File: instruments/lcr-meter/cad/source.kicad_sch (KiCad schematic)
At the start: 19 parts, among them U4 AD9833BRMZ-REEL7, U5 OPA810IDBVR

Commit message: lcr-meter Rev D: apply Tier 1 audit fixes
Hand-routed layout edits (cad/tools/edit_lib.py, no autorouter):
- Vias in every exposed pad: U1 8, U8/U9/U10 5, U11/U12 6 (were 0), U13 9.
- ADS9224R: 10 uF X7R 0805 reference caps at 1.56 mm, REFM joined to the
  cap before its via; 1 uF AVDD caps at 1.67/2.46 mm from pins 12/29.
- TPS7A4901/TPS7A3001: support parts packed per TI layout; FB nodes
  13.2/12.0 -> 5.2/5.3 mm, NR 2.1 mm. LDOIN_N In2 run moved off the pads.
- TPS65131 dividers compacted: CONV_FBP 13.1 -> 9.1 mm, CONV_FBN 16.8 -> 12.3 mm.
- RP2040: 1 uF at VREG_VIN (C5).

Parts: red status LED, basic ferrites, W25Q128JV flash (stock), C84,
CL32B106KBJNNNE on the 14 V and converter-input caps, C18/C103 basic,
C36 1 uF -> 100 nF. Extended lines 34 -> 30.

Firmware: settle max(150 ms, 20 cycles); BOOT -> reset_usb_boot().
Host 0.7.0: `temper-lcr boot PORT`.

Withdrawn after checking: converter dividers to TI example values (VPOS
15.105 V at the tolerance stack), 1 % LDO dividers (U12 headroom 0.74 V),
SRV05-4 (pinout unverifiable). regulator_check.py now reads design.json
instead of stale Rev C values.

DRC 0, unconnected 0, parity 0, ERC 0; independent check 576 pins, 0
findings; host 29 tests pass.

Co-Authored-By: Claude Opus 5.5 <noreply@anthropic.com>
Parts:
- C36: value 1uF 50V -> 100nF 50V; LCSC C28323 -> C49678; MPN CL21B105KBFNNNE -> CC0805KRX7R9BB104; Manufacturer Samsung Electro-Mechanics -> YAGEO; Unit_USD 0.0344 -> 0.015
- FB2: value 120R@100MHz 3A -> 100R@100MHz 800mA; LCSC C79382 -> C1015; MPN BLM21PG121SN1D -> GZ2012D101TF; Manufacturer Murata Electronics -> Sunlord; Unit_USD 0.0406 -> 0.0311

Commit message: feat(lcr): Rev E board with TAC5112 codec front end and relay ranges
Hand-routed Rev E on the Rev D outline:
- removes the ADS9224R, AD9833, both THS4551s, FB2 and JP1-JP6;
- adds the TAC5112 with its own AP2112K for 3V3A, three TQ2SA latching
  relays and their AO3400A drivers.

cad/tools/rev_e.py builds design.json and routing.json from the Rev D
package. rev_e_routes.py gives every new segment and via by coordinate.

Details:
- Every via is now a 0.3 mm drill with a pad of 0.45 mm or more.
  The board rules set a 0.30 mm minimum hole and a 0.075 mm minimum
  annular ring.
- Basic-library swaps: D1 is now SRV05-4, and SW1/SW2 are now TS-1088.
- placement_offsets.py adds JLC CPL offsets for the new keyed parts,
  read from the lceda.cn EasyEDA mirror (easyeda.com returns 403). It
  reproduces the audited offsets for U3 (270) and Q1 (180).

Checks:
- rebuild.sh: ERC 0, DRC 0 violations and 0 unconnected, parity 0.
- package_cad and audit_dfm pass: 34 intended via-in-pad, none
  unexpected.
- independent_check.py e: 575 pins, 0 findings.

Co-Authored-By: Claude Opus 5.5 <noreply@anthropic.com>
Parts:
- removed C30: 10nF 50V, LCR:C_0603_1608Metric, symbol LCR:C
- removed C31, C32: 100nF 50V, LCR:C_0603_1608Metric, symbol LCR:C
- removed C33: 1uF 50V, LCR:C_0805_2012Metric, symbol LCR:C
- removed C36: 100nF 50V, LCR:C_0805_2012Metric, symbol LCR:C
- removed FB2: 100R@100MHz 800mA, LCR:L_0805_2012Metric, symbol LCR:L
- removed R34: 1k 0.1%, LCR:R_0603_1608Metric, symbol LCR:R
- removed U4: AD9833BRMZ-REEL7, LCR:MSOP-10_3x3mm_P0.5mm, symbol LCR:AD9833
- C34, C35: value 1nF C0G -> 270pF C0G 5%; LCSC C106246 -> C107046; MPN CC0603JRNPO9BN102 -> CC0603JRNPO9BN271; Unit_USD 0.0057 -> 0.0092
- R30, R31: value 330R -> 2.2k 0.1%; LCSC C23138 -> C861295; MPN 0603WAF3300T5E -> RT0603BRD072K2L; Manufacturer UNI-ROYAL(Uniroyal Elec) -> YAGEO; Unit_USD 0.002 -> 0.0363
- R32: value 100k -> 2k 0.1%; LCSC C25803 -> C728588; MPN 0603WAF1003T5E -> RT0603BRD072KL; Manufacturer UNI-ROYAL(Uniroyal Elec) -> YAGEO; Unit_USD 0.0031 -> 0.035
- R33: value 5k 0.1% -> 2k 0.1%; LCSC C862232 -> C728588; MPN RT0603BRE075KL -> RT0603BRD072KL; Unit_USD 0.0262 -> 0.035
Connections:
- net EXCITE: now also C35.1
- net GND: no longer C35.2
- net SOURCE_AC: now also C34.1, R30.2
- net SOURCE_FB: now also C35.2, R31.1
- net DDS_OUT renamed DAC_P
- removed net LP1: C34.1, R30.2, R31.1
- net LP2 renamed DAC_M
- net DAC_M: no longer C35.1
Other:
- note added: "TAC5112 OUT1P/OUT1M differential line out at fs = 187.5kHz. OPA810 difference stage: 2.2k in, 2.0k || 270pF feedback and ground leg, gain 0.909. DC coupled: the stage rejects the 1.65V DAC common mode."
- note removed: "24MHz DDS clock from RP2040 120MHz / 5; sine output only. Two 330R/1nF RC stages, AC coupling, OPA810 noninverting gain 6. This block is added to the TI reference. Measure actual amplitude and distortion."
- title: DDS excitation and reconstruction -> Codec DAC excitation
- moved on the sheet: C34, C35, C37, C38, C39, C40, R30, R31, R32, R33, U5

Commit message: lcr-meter: Rev E cost pass: tented vias (no POFV), two extended lines freed, 2k/5k 0.1 % restocked at 25 ppm
Five vias moved off small SMT lands (R3.2, C44.1, R101.1, U16.2, Y1.4); the 33
exposed-pad thermal vias stay, tented on B.Mask. audit_dfm.py now fails on a via
ring touching a land and on any untented via. Boost divider 430k/40.2k with 15 pF
and 4.7 pF feed-forward (preferred/basic). R32/R33 and R41/R44 move to Viking
25 ppm/C thin film (C728588 down to 22 in stock; the 5k was 50 ppm/C against the
budget). ERC 0, DRC 0/0/0, independent check 0, layout audit unchanged.
Five boards: $458.02 -> $428.40.

Co-Authored-By: Claude Opus 5.5 <noreply@anthropic.com>
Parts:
- R32, R33: LCSC C728588 -> C318130; MPN RT0603BRD072KL -> AR03BTCX2001; Manufacturer YAGEO -> Viking Tech; Unit_USD 0.035 -> 0.0364

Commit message: lcr-meter: Rev E consolidates four extended lines and moves U2 to a 2 MB flash
LDO dividers: U11 82k/9.1k 1 % basic; U12 100k over 5k+1k+5k from 0.1 % lines
already on the BOM (R112 added). C34/C35 270 pF built as two 560 pF in series
(C114/C115). R83 1.74M built as 240k + 1.5M (R111). U2 W25Q128JVSIQ ->
GD25Q16ESIGR, same SOP-8 208 mil land, CPL offset unchanged.

regulator_check reads divider strings from the netlist and adds a TCR row:
45 of 46 pass; R95/R96 headroom 1.083 V (was the 0.951 V FLAG); the new TCR row
flags 0.970 V (0.838 V on the old dividers). New source_stage.py: U5 margin
59.73 deg (60.13), -0.025 dB at 85 kHz. ERC 0, DRC 0/0/0, independent check
632 pins 0 findings. 23 extended lines; five boards $428.40 -> $408.57.

Co-Authored-By: Claude Opus 5.5 <noreply@anthropic.com>
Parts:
- added C114, C115: 560pF C0G 5%, LCR:C_0603_1608Metric, symbol LCR:C
- C34, C35: value 270pF C0G 5% -> 560pF C0G 5%; LCSC C107046 -> C107054; MPN CC0603JRNPO9BN271 -> CC0603JRNPO9BN561; Unit_USD 0.0092 -> 0.0066
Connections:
- net EXCITE: now also C115.1; no longer C35.1
- net GND: now also C114.2; no longer C34.2
- new net SRC_AC_CMID: C114.1, C34.2
- new net SRC_FB_CMID: C115.2, C35.1
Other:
- note added: "TAC5112 OUT1P/OUT1M differential line out at fs = 187.5kHz. OPA810 difference stage: 2.2k in, 2.0k || 280pF (2 x 560pF in series) feedback and ground leg, gain 0.909. DC coupled: the stage rejects the 1.65V DAC common mode."
- note removed: "TAC5112 OUT1P/OUT1M differential line out at fs = 187.5kHz. OPA810 difference stage: 2.2k in, 2.0k || 270pF feedback and ground leg, gain 0.909. DC coupled: the stage rejects the 1.65V DAC common mode."
- moved on the sheet: C35

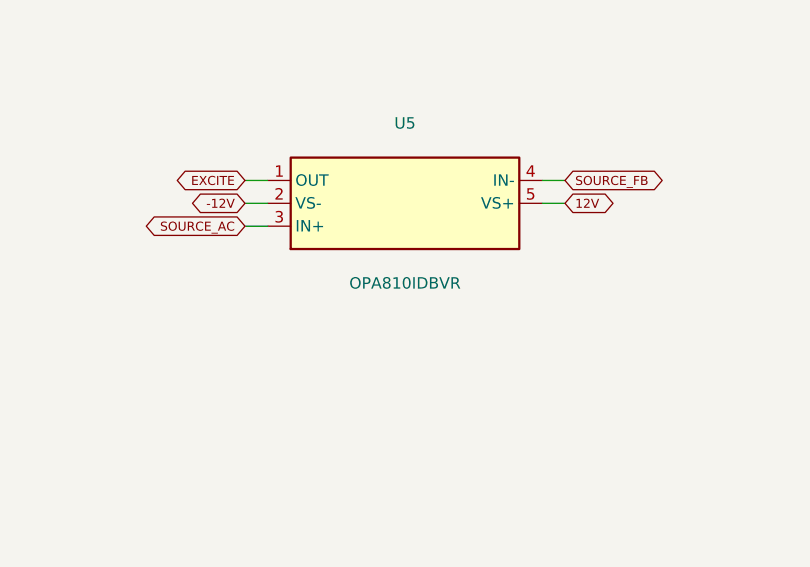
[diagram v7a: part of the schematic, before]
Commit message: lcr-meter: U5 OPA810 -> OPA197 (same SOT-23-5 pinout), CPL offset 180
source_stage.py runs U5 as the OPA810 or TI's OPAx197 model (SBOMA35) and
records each part's DAC -> SOURCE transfer to 30 MHz: OPA197 loop 67.81 deg
(OPA810 60.11), 0.3-1.7 dB less attenuation at 4-16 MHz. dac_images_u5.py puts
that transfer in place of rev_e_spurs' ideal pole: image error on a 27 kHz coil
0.724 % vs 0.704 % at 16 fs. The JLC land record for C221351 is 180 deg from
KiCad's, so the CPL angle is 180. OPA2197 for U6/U7 recorded as not taken.
ERC 0, DRC 0/0/0, independent check 0. Five boards $396.25 -> $385.65.

Co-Authored-By: Claude Opus 5.5 <noreply@anthropic.com>
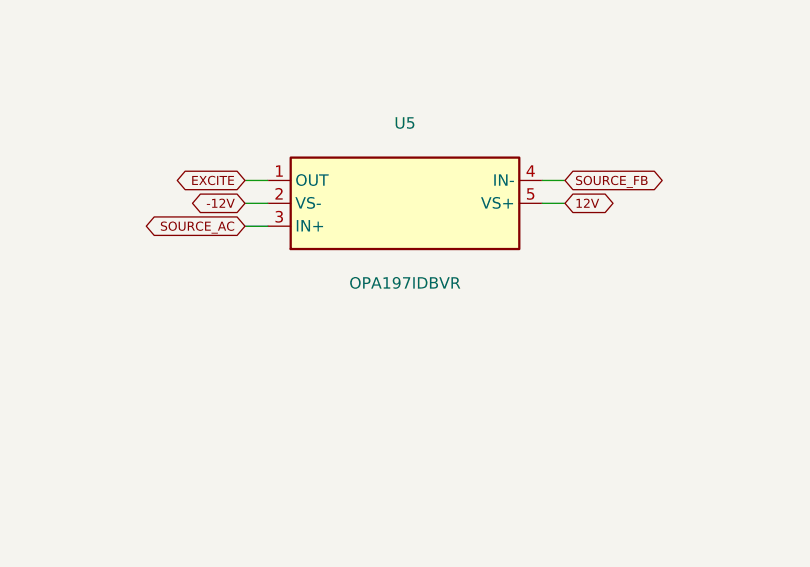
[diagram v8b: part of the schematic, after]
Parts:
- U5: value OPA810IDBVR -> OPA197IDBVR; LCSC C2833513 -> C221351; MPN OPA810IDBVR -> OPA197IDBVR; Unit_USD 3.0949 -> 0.5978
